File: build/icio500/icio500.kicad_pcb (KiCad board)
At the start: 4 copper layers, 150.8 x 114.3 mm, 56 parts, among them J1 ?, U1 ?, U2 ?, U3 ?, U4 ?, U5 ?, U6 ?

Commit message: idk
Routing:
- net gpio_enc_sw: track 57.0 -> 189.0 mm, vias 0 -> 3
- net gpio_enc_b: track 57.8 -> 188.2 mm, vias 0 -> 3
- net d14: track 53.4 -> 179.7 mm, vias 0 -> 3
- net d13: track 52.7 -> 177.4 mm, vias 0 -> 3
- net gpio_disp_dc: track 73.4 -> 197.6 mm, vias 0 -> 3
- net spi1_cs: track 68.2 -> 188.8 mm, vias 1 -> 4
- net spi1_mosi: track 64.8 -> 184.9 mm, vias 0 -> 3
- net spi1_sck: track 68.3 -> 187.9 mm, vias 0 -> 3
- net spi1_miso: track 60.7 -> 179.3 mm, vias 0 -> 3
- net i2c1_sda: track 67.3 -> 185.1 mm, vias 0 -> 3
- net gpio_disp_res: track 73.9 -> 188.9 mm, vias 1 -> 4
- net i2c1_scl: track 71.9 -> 186.0 mm, vias 1 -> 4
- net audio_in_r: track 106.6 -> 191.2 mm, vias 1 -> 4
- net daisy_5v_power: track 152.1 -> 230.7 mm, vias 0 -> 3

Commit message: multistep error check and fixing
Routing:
- net gnd: track 235.5 -> 127.7 mm, vias 25 -> 28
- net audio_in_r: track 191.2 -> 86.1 mm, vias 4 -> 3
- net daisy_5v_power: track 230.7 -> 135.0 mm, vias 3 -> 2
- net gpio_enc_sw: track 189.0 -> 102.0 mm
- net gpio_disp_dc: track 197.6 -> 112.5 mm
- net gpio_disp_res: track 188.9 -> 105.4 mm, vias 4 -> 3
- net spi1_cs: track 188.8 -> 106.9 mm, vias 4 -> 3
- net gpio_enc_b: track 188.2 -> 110.2 mm
- net d14: track 179.7 -> 105.6 mm
- net spi1_sck: track 187.9 -> 114.0 mm
- net spi1_miso: track 179.3 -> 108.3 mm
- net spi1_mosi: track 184.9 -> 115.4 mm
- net d13: track 177.4 -> 113.8 mm
- net i2c1_scl: track 186.0 -> 122.5 mm, vias 4 -> 3
- net i2c1_sda: track 185.1 -> 124.5 mm

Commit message: attemptin to confor to vpr specs
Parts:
- moved U5 42.4 mm to (95.0, 90.0), turned to 0 degrees
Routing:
- net i2c1_sda: track 124.5 -> 41.5 mm, vias 3 -> 0
- net i2c1_scl: track 122.5 -> 41.5 mm, vias 3 -> 0
- net spi1_mosi: track 115.4 -> 43.6 mm, vias 3 -> 0
- net spi1_sck: track 114.0 -> 42.6 mm, vias 3 -> 0
- net gpio_disp_dc: track 112.5 -> 41.5 mm, vias 3 -> 0
- net gnd: track 127.7 -> 57.5 mm, vias 28 -> 26
- net spi1_miso: track 108.3 -> 41.1 mm, vias 3 -> 0
- net d13: track 113.8 -> 46.8 mm, vias 3 -> 0
- net spi1_cs: track 106.9 -> 40.1 mm, vias 3 -> 0
- net gpio_disp_res: track 105.4 -> 39.0 mm, vias 3 -> 0
- net audio_in_r: track 86.1 -> 146.7 mm, vias 3 -> 0
- net gpio_enc_b: track 110.2 -> 50.0 mm, vias 3 -> 0
- net daisy_5v_power: track 135.0 -> 194.6 mm, vias 2 -> 1
- net d14: track 105.6 -> 46.4 mm, vias 3 -> 0
- net gpio_enc_sw: track 102.0 -> 49.5 mm, vias 3 -> 0
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
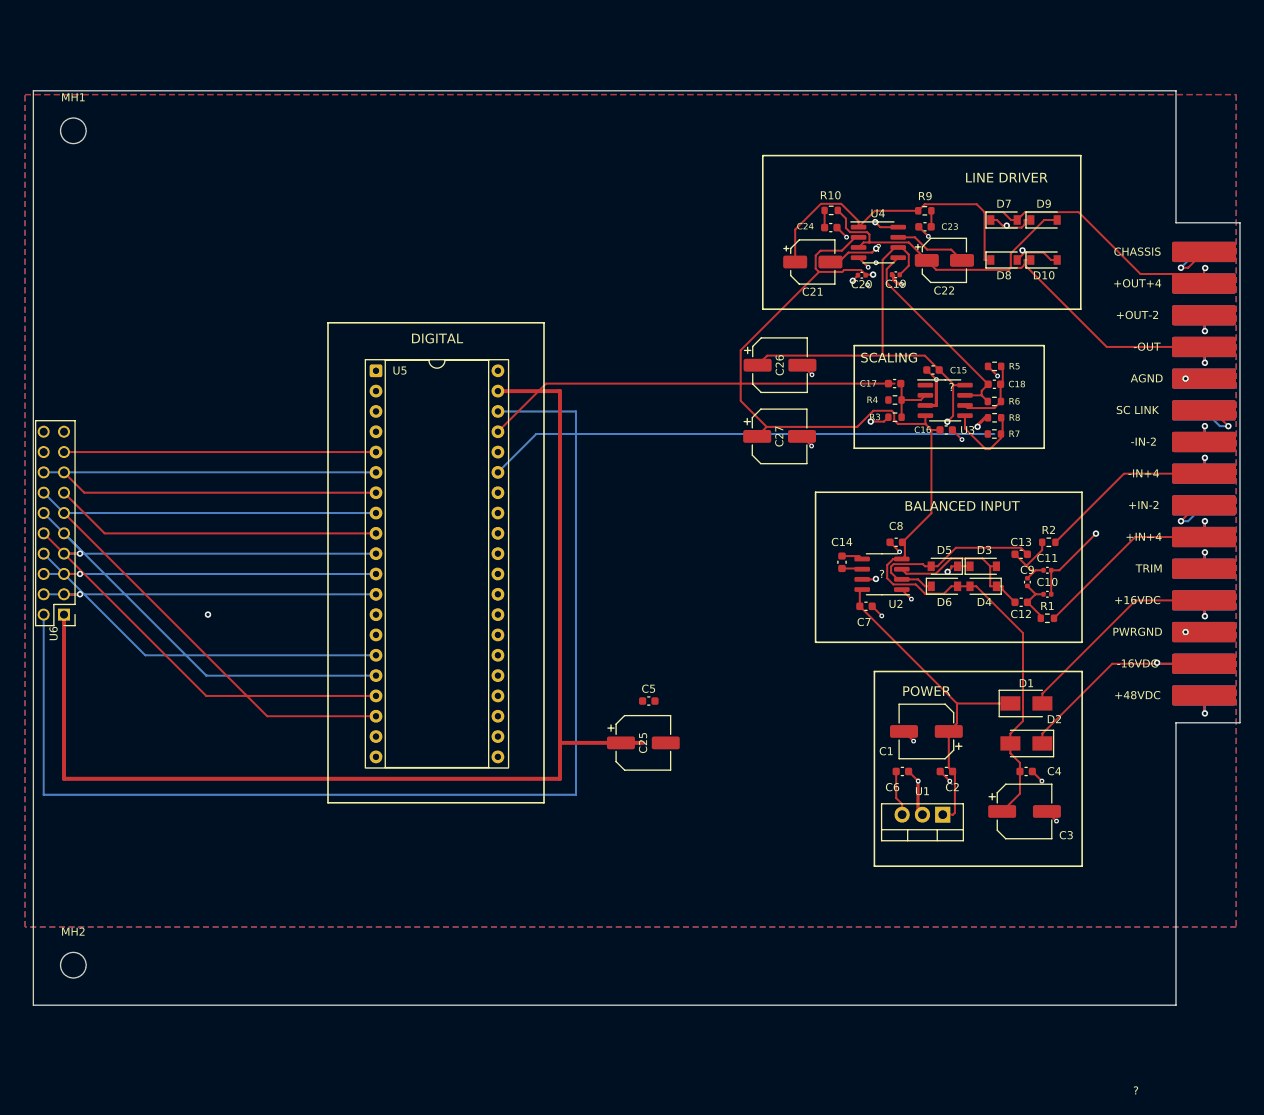
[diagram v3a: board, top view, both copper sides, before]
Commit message: Restore VPR summer board outline (Y=160mm, 26mm bottom notch), align lower bracket BR2, purge vestigial files
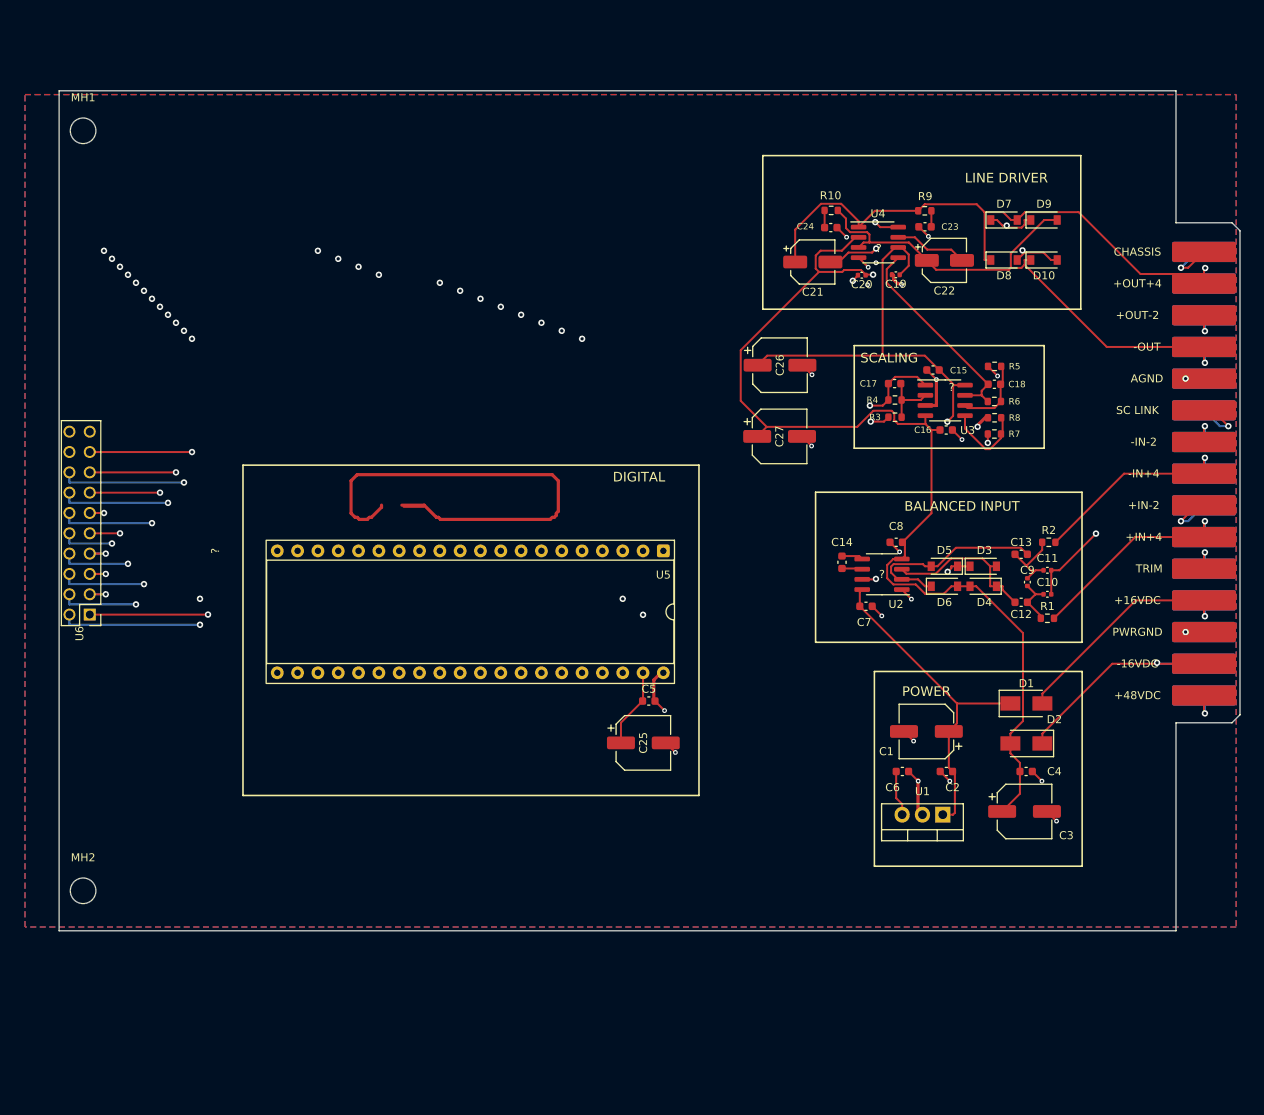
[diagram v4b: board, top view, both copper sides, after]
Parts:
- moved U5 42.4 mm to (130.9, 112.5), turned to -90 degrees
- moved MH2 9.38 mm to (58.4, 155.0)
- moved U6 3.22 mm to (59.2, 120.5)
- moved MH1 1.22 mm to (58.4, 60.0)
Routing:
- net i2c1_sda: track 41.5 -> 121.3 mm, vias 0 -> 3
- net i2c1_scl: track 41.5 -> 119.3 mm, vias 0 -> 3
- net gnd: track 57.5 -> 127.7 mm, vias 26 -> 28
- net spi1_mosi: track 43.6 -> 112.2 mm, vias 0 -> 3
- net spi1_sck: track 42.6 -> 110.7 mm, vias 0 -> 3
- net gpio_disp_dc: track 41.5 -> 109.3 mm, vias 0 -> 3
- net spi1_miso: track 41.1 -> 105.1 mm, vias 0 -> 3
- net audio_in_r: track 146.7 -> 82.9 mm, vias 0 -> 3
- net d13: track 46.8 -> 110.6 mm, vias 0 -> 3
- net spi1_cs: track 40.1 -> 103.7 mm, vias 0 -> 3
- net gpio_disp_res: track 39.0 -> 102.2 mm, vias 0 -> 3
- net daisy_5v_power: track 194.6 -> 131.8 mm, vias 1 -> 2
- net gpio_enc_b: track 50.0 -> 107.0 mm, vias 0 -> 3
- net d14: track 46.4 -> 102.4 mm, vias 0 -> 3
- net gpio_enc_sw: track 49.5 -> 98.8 mm, vias 0 -> 3
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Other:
- board size 150.8 x 114.3 mm -> 147.6 x 105 mm

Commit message: Rotate Daisy 90 deg CCW, route 0-DRC digital bus, and fix faceplate mechanical mating
- Restore Daisy Seed U5 vertical orientation (at 95 90 0) and DIGITAL silkscreen frame
- Route multilayer planar traces for all 12 U6-U5 digital nets, 5V power, and audio signals with 0 DRC violations and 0 unconnected items
- Fix 3D assembly offsets in scripts/make_assemblies.py for flush mating of main card, satellite board, and front faceplate
- Scale U6 3D model X axis to 0.5 to keep right-angle male pins seated inside socket J1 without faceplate protrusion
- Re-export JLCPCB fabrication packages and render assembly views
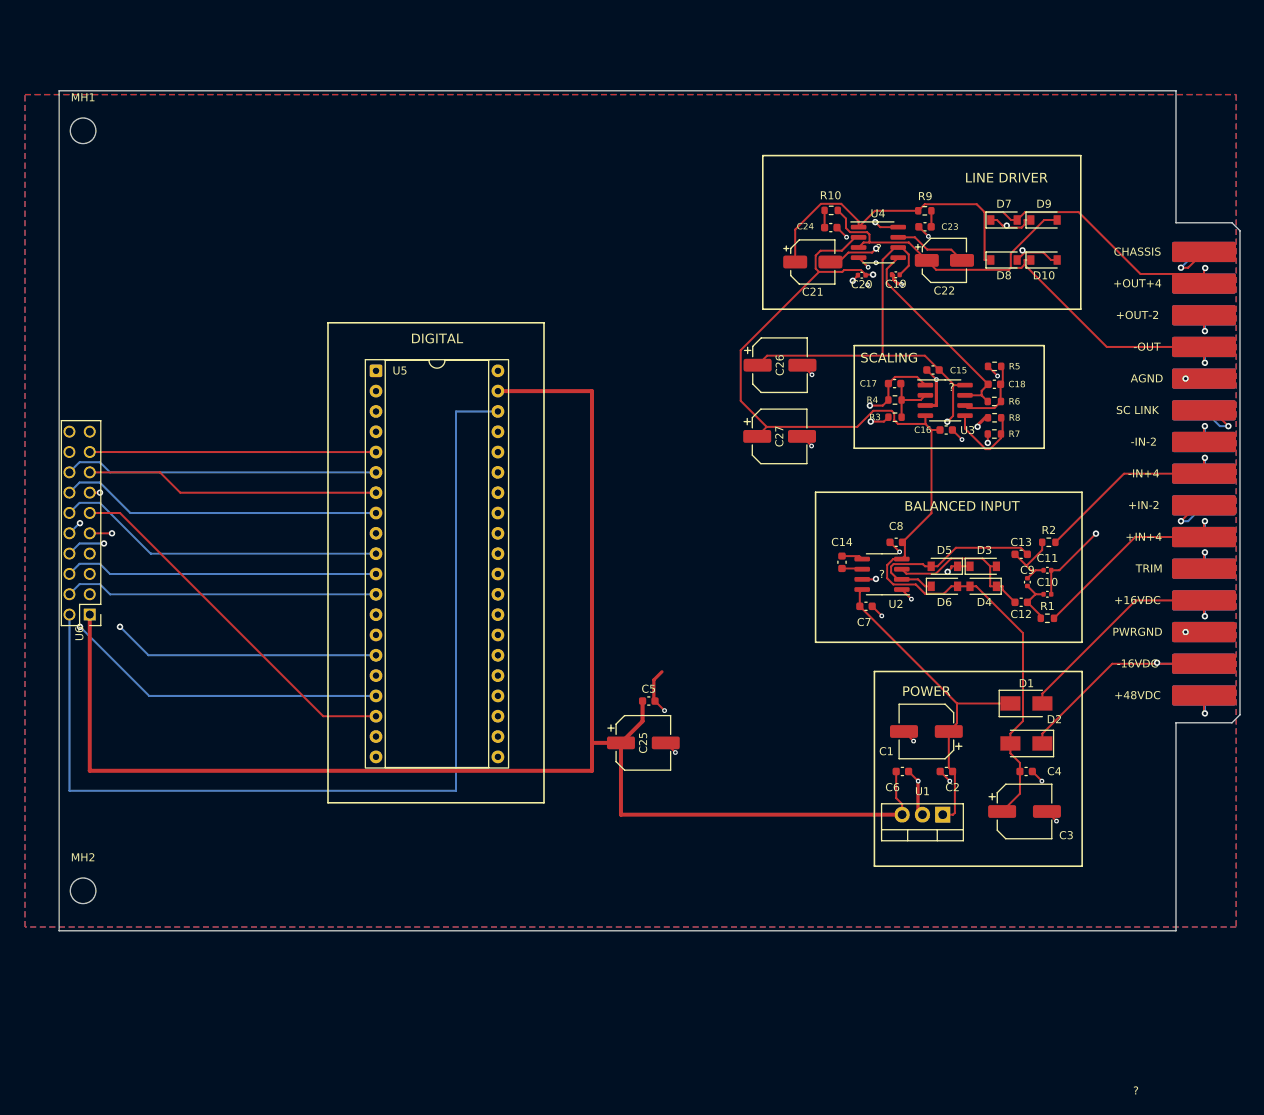
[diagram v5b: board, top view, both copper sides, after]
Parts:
- moved U5 42.4 mm to (95.0, 90.0), turned to 0 degrees
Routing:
- net i2c1_sda: track 121.3 -> 39.4 mm, vias 3 -> 0
- net i2c1_scl: track 119.3 -> 39.4 mm, vias 3 -> 0
- net gnd: track 127.7 -> 52.8 mm, vias 28 -> 25
- net spi1_mosi: track 112.2 -> 41.5 mm, vias 3 -> 0
- net spi1_sck: track 110.7 -> 40.4 mm, vias 3 -> 0
- net gpio_disp_dc: track 109.3 -> 39.4 mm, vias 3 -> 0
- net daisy_5v_power: track 131.8 -> 201.3 mm, vias 2 -> 0
- net spi1_miso: track 105.1 -> 37.9 mm, vias 3 -> 1
- net spi1_cs: track 103.7 -> 36.8 mm, vias 3 -> 0
- net gpio_disp_res: track 102.2 -> 35.8 mm, vias 3 -> 0
- net d13: track 110.6 -> 50.7 mm, vias 3 -> 2
- net d14: track 102.4 -> 47.6 mm, vias 3 -> 1
- net gpio_enc_sw: track 98.8 -> 46.3 mm, vias 3 -> 0
- net gpio_enc_b: track 107.0 -> 55.4 mm, vias 3 -> 2
- net audio_in_r: track 82.9 -> 123.0 mm, vias 3 -> 0
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
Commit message: Finalize VPR-500 mechanical mating, zero-DRC routing, unit 3D model scale, and JLCPCB packages
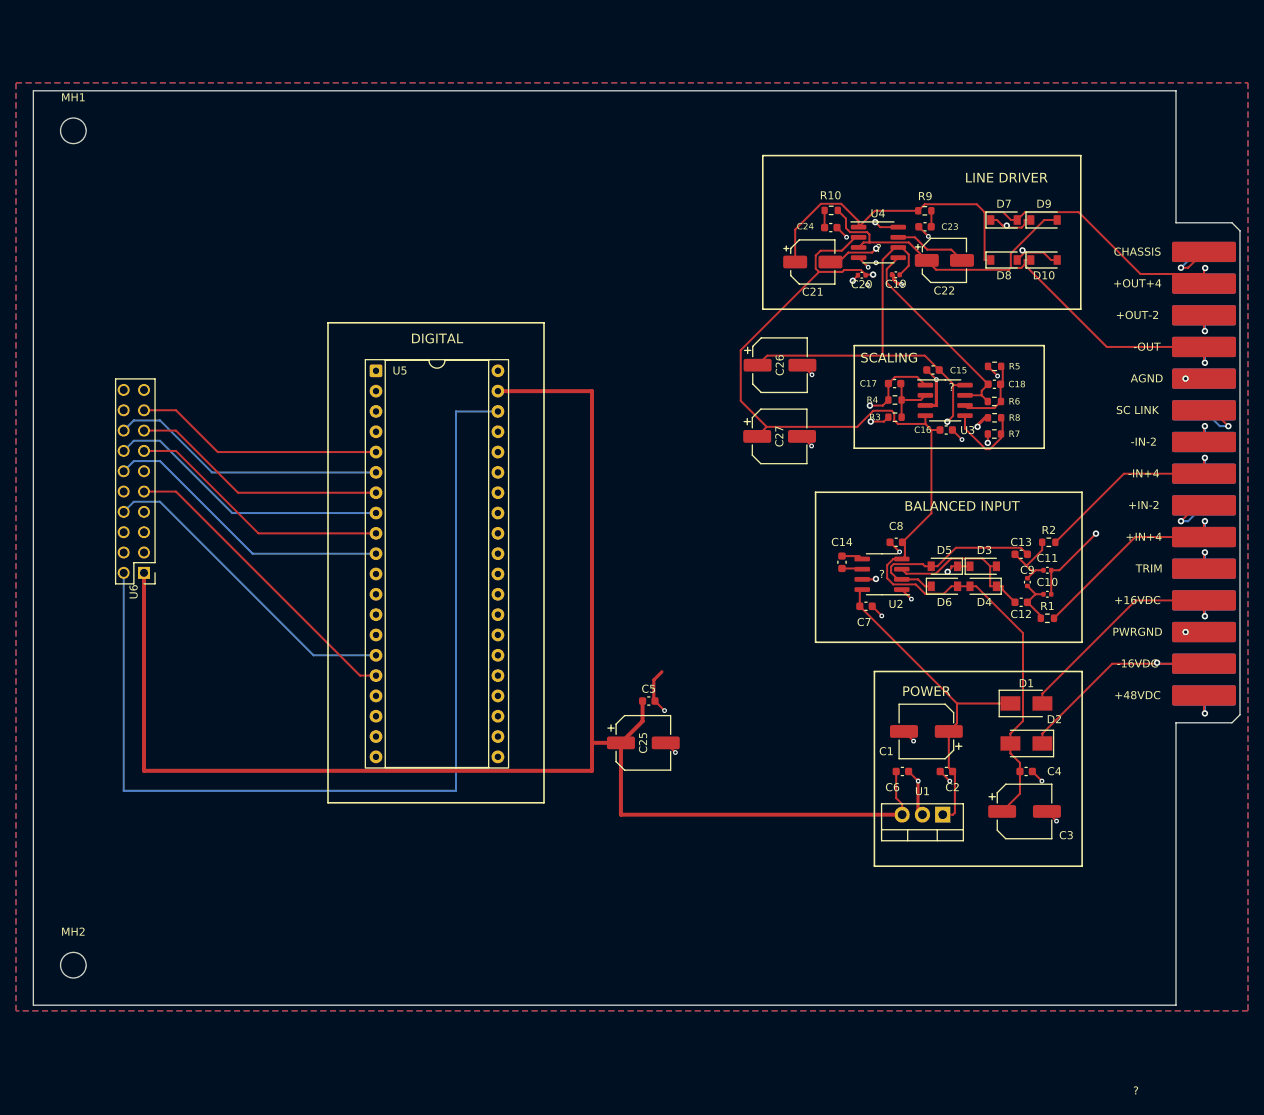
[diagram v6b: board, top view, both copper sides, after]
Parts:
- moved MH2 9.38 mm to (57.2, 164.3)
- moved U6 8.55 mm to (66.0, 115.3)
- moved MH1 1.22 mm to (57.2, 60.0)
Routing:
- net gpio_enc_sw: track 46.3 -> 80.4 mm
- net gpio_enc_b: track 55.4 -> 69.0 mm, vias 2 -> 0
- net d13: track 50.7 -> 40.0 mm, vias 2 -> 0
- net d14: track 47.6 -> 38.5 mm, vias 1 -> 0
- net i2c1_scl: track 39.4 -> 34.8 mm
- net gpio_disp_dc: track 39.4 -> 34.8 mm
- net i2c1_sda: track 39.4 -> 34.8 mm
- net spi1_sck: track 40.4 -> 35.8 mm
- net spi1_mosi: track 41.5 -> 36.9 mm
- net spi1_miso: track 37.9 -> 33.3 mm, vias 1 -> 0
- net spi1_cs: track 36.8 -> 32.2 mm
- net gpio_disp_res: track 35.8 -> 31.2 mm
- net audio_in_r: track 123.0 -> 121.4 mm
- net daisy_5v_power: track 201.3 -> 199.8 mm
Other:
- board size 147.6 x 105 mm -> 150.8 x 114.3 mm

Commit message: Restore authentic VPR-500 carrier board outline (Y=55-160mm, 26mm notch) and concentric 3-point mating
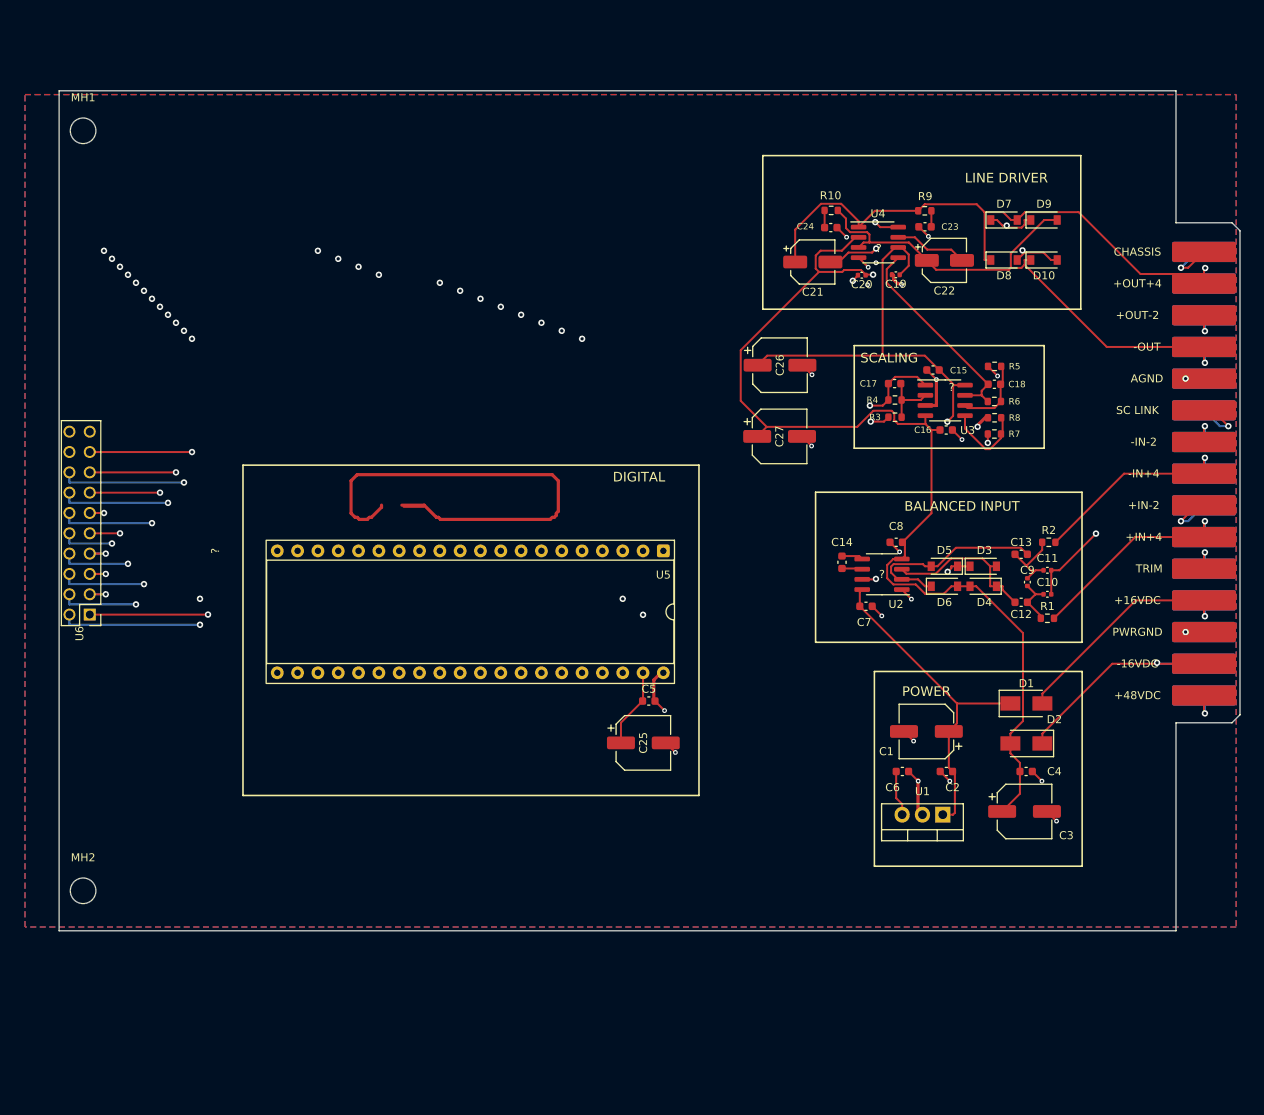
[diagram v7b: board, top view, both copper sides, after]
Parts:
- moved U5 42.4 mm to (130.9, 112.5), turned to -90 degrees
- moved MH2 9.38 mm to (58.4, 155.0)
- moved U6 8.55 mm to (59.2, 120.5)
- moved MH1 1.22 mm to (58.4, 60.0)
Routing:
- net i2c1_sda: track 34.8 -> 121.3 mm, vias 0 -> 3
- net i2c1_scl: track 34.8 -> 119.3 mm, vias 0 -> 3
- net spi1_mosi: track 36.9 -> 112.2 mm, vias 0 -> 3
- net spi1_sck: track 35.8 -> 110.7 mm, vias 0 -> 3
- net gnd: track 52.8 -> 127.7 mm, vias 25 -> 28
- net gpio_disp_dc: track 34.8 -> 109.3 mm, vias 0 -> 3
- net spi1_miso: track 33.3 -> 105.1 mm, vias 0 -> 3
- net spi1_cs: track 32.2 -> 103.7 mm, vias 0 -> 3
- net gpio_disp_res: track 31.2 -> 102.2 mm, vias 0 -> 3
- net d13: track 40.0 -> 110.6 mm, vias 0 -> 3
- net daisy_5v_power: track 199.8 -> 131.8 mm, vias 0 -> 2
- net d14: track 38.5 -> 102.4 mm, vias 0 -> 3
- net audio_in_r: track 121.4 -> 82.9 mm, vias 0 -> 3
- net gpio_enc_b: track 69.0 -> 107.0 mm, vias 0 -> 3
- net gpio_enc_sw: track 80.4 -> 98.8 mm, vias 0 -> 3
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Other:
- board size 150.8 x 114.3 mm -> 147.6 x 105 mm
